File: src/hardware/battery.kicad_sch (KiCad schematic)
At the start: 1 part

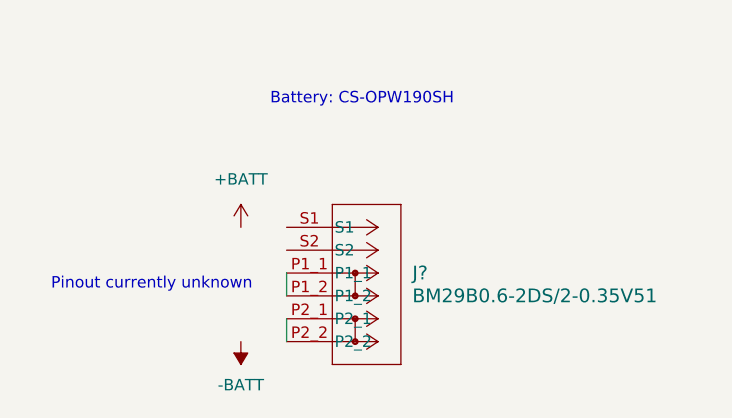
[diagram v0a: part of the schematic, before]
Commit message: Cleanup & Fixes; Added footprints; Removed Light sensors
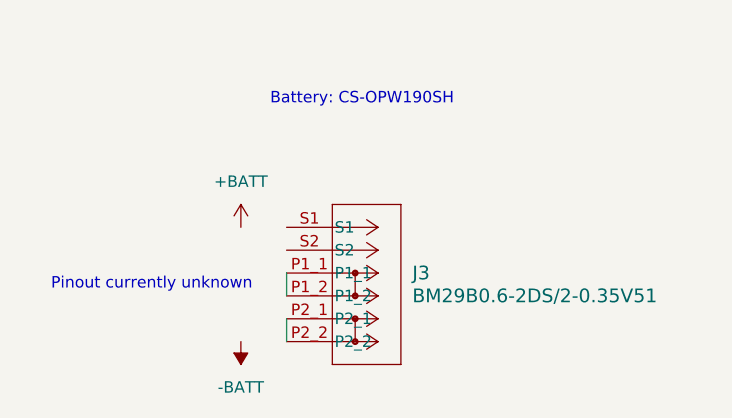
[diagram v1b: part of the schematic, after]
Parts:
- J3: renamed from J?; footprint CONN_BM29B0.6-2DS/2-0.35V51_HIR -> Project:CONN_BM29B0.6-2DS&slash_2-0.35V51_HIR
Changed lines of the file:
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@@
 		(dnp no)
 		(fields_autoplaced yes)
-		(property "Reference" "J?"
+		(property "Reference" "J3"
 			(at 157.48 100.3299 0)
 			(effects
@@
 			)
 		)
-		(property "Footprint" "CONN_BM29B0.6-2DS/2-0.35V51_HIR"
+		(property "Footprint" "Project:CONN_BM29B0.6-2DS&slash_2-0.35V51_HIR"
 			(at 143.51 95.25 0)
 			(effects
@@
 			(project "raywatch"
 				(path "/7b654ee8-2a53-4d39-8b7d-32c7bb3cb0ed/6e6a70ea-4db2-4b59-a2d7-c468f9b8b5a6/0e8527e5-475a-4be8-8e89-500ec2c68fe4"
-					(reference "J?")
+					(reference "J3")
 					(unit 1)
 				)
@@
 		(dnp no)
 		(fields_autoplaced yes)
-		(property "Reference" "#PWR0401"
+		(property "Reference" "#PWR0404"
 			(at 138.43 99.06 0)
 			(effects
@@
 		)
 		(property "Value" "+BATT"
-			(at 138.43 89.916 0)
+			(at 138.43 90.17 0)
 			(effects
 				(font
@@
 			(project "raywatch"
 				(path "/7b654ee8-2a53-4d39-8b7d-32c7bb3cb0ed/6e6a70ea-4db2-4b59-a2d7-c468f9b8b5a6/0e8527e5-475a-4be8-8e89-500ec2c68fe4"
-					(reference "#PWR0401")
+					(reference "#PWR0404")
 					(unit 1)
 				)
@@
 		(dnp no)
 		(fields_autoplaced yes)
-		(property "Reference" "#PWR0402"
+		(property "Reference" "#PWR0405"
 			(at 138.43 104.14 0)
 			(effects
@@
 		)
 		(property "Value" "-BATT"
-			(at 138.43 112.776 0)
+			(at 138.43 113.03 0)
 			(effects
 				(font
@@
 			(project "raywatch"
 				(path "/7b654ee8-2a53-4d39-8b7d-32c7bb3cb0ed/6e6a70ea-4db2-4b59-a2d7-c468f9b8b5a6/0e8527e5-475a-4be8-8e89-500ec2c68fe4"
-					(reference "#PWR0402")
+					(reference "#PWR0405")
 					(unit 1)
 				)

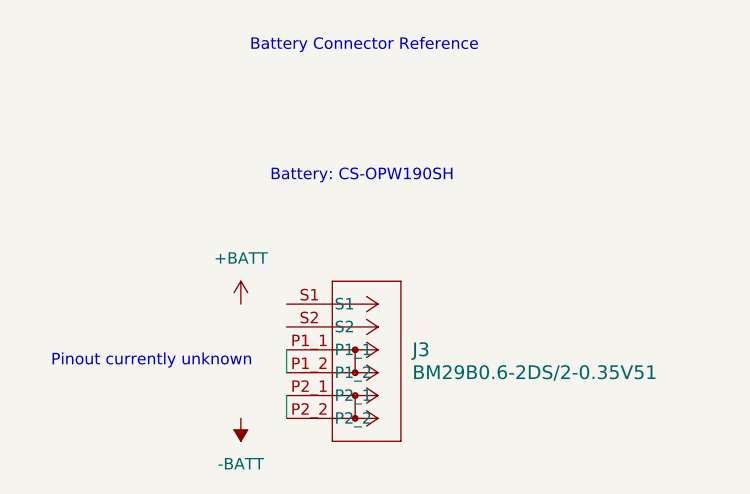
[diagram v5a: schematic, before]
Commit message: Mapped battery pinout; Removed thermistor from PCB, now using thermistor in battery pack
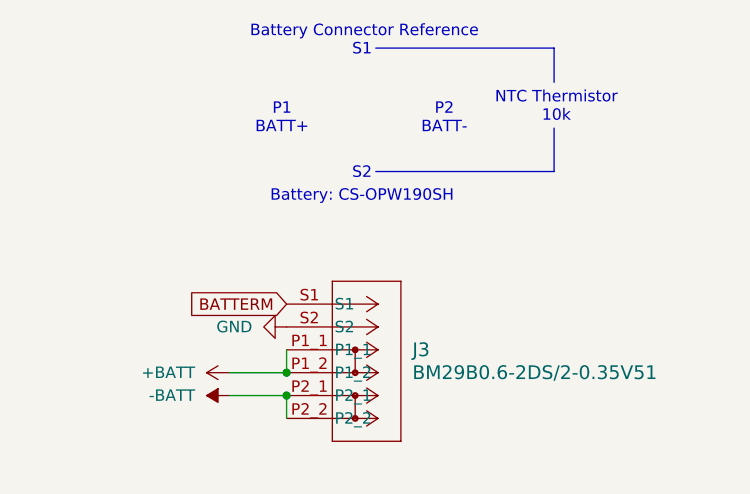
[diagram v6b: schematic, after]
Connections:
- net +BATT: now also J3.P1_1, J3.P1_2
- net -BATT: now also J3.P2_1, J3.P2_2
- net BATTERM: now reaches J3.S1
- net GND: now reaches J3.S2
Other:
- note added: "NTC Thermistor 10k"
- note added: "P1 BATT+"
- note added: "P2 BATT-"
- note added: "S1"
- note added: "S2"
- note removed: "Pinout currently unknown"
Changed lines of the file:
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@@
 		(date "2026-10-21")
 	)
-	(text "Battery: CS-OPW190SH"
-		(exclude_from_sim no)
-		(at 151.892 81.026 0)
+	(text "S1"
+		(exclude_from_sim no)
+		(at 151.892 67.056 0)
 		(effects
 			(font
@@
 		)
 	)
-	(text "Pinout currently unknown"
-		(exclude_from_sim no)
-		(at 128.524 101.6 0)
+	(text "Battery: CS-OPW190SH"
+		(exclude_from_sim no)
+		(at 151.892 83.312 0)
 		(effects
 			(font
@@
 	(text "Battery Connector Reference"
 		(exclude_from_sim no)
-		(at 152.146 66.548 0)
+		(at 152.146 65.024 0)
 		(effects
 			(font
@@
 		)
 	)
+	(text "NTC Thermistor\n10k"
+		(exclude_from_sim no)
+		(at 173.482 73.406 0)
+		(effects
+			(font
+				(size 1.27 1.27)
+			)
+		)
+	)
+	(text "S2"
+		(exclude_from_sim no)
+		(at 151.892 80.772 0)
+		(effects
+			(font
+				(size 1.27 1.27)
+			)
+		)
+	)
+	(text "P1\nBATT+"
+		(exclude_from_sim no)
+		(at 143.002 74.676 0)
+		(effects
+			(font
+				(size 1.27 1.27)
+			)
+		)
+	)
+	(text "P2\nBATT-"
+		(exclude_from_sim no)
+		(at 161.036 74.676 0)
+		(effects
+			(font
+				(size 1.27 1.27)
+			)
+		)
+	)
+	(junction
+		(at 143.51 102.87)
+		(diameter 0)
+		(color 0 0 0 0)
+	)
+	(junction
+		(at 143.51 105.41)
+		(diameter 0)
+		(color 0 0 0 0)
+	)
+	(wire
+		(pts
+			(xy 137.16 105.41) (xy 143.51 105.41)
+		)
+		(stroke
+			(width 0)
+			(type default)
+		)
+	)
+	(wire
+		(pts
+			(xy 137.16 102.87) (xy 143.51 102.87)
+		)
+		(stroke
+			(width 0)
+			(type default)
+		)
+	)
+	(wire
+		(pts
+			(xy 143.51 102.87) (xy 143.51 100.33)
+		)
+		(stroke
+			(width 0)
+			(type default)
+		)
+	)
+	(polyline
+		(pts
+			(xy 173.228 66.802) (xy 153.416 66.802)
+		)
+		(stroke
+			(width 0)
+			(type default)
+		)
+	)
+	(polyline
+		(pts
+			(xy 173.228 80.518) (xy 173.228 75.692)
+		)
+		(stroke
+			(width 0)
+			(type default)
+		)
+	)
 	(wire
 		(pts
@@
 		)
 	)
-	(wire
+	(polyline
 		(pts
-			(xy 143.51 100.33) (xy 143.51 102.87)
+			(xy 153.416 80.518) (xy 173.228 80.518)
+		)
+		(stroke
+			(width 0)
+			(type default)
+		)
+	)
+	(polyline
+		(pts
+			(xy 173.228 70.612) (xy 173.228 66.802)
 		)
 		(stroke
@@
 		)
 	)
+	(global_label "BATTERM"
+		(shape input)
+		(at 143.51 95.25 180)
+		(fields_autoplaced yes)
+		(effects
+			(font
+				(size 1.27 1.27)
+			)
+			(justify right)
+		)
+		(property "Intersheetrefs" "${INTERSHEET_REFS}"
+			(at 132.3606 95.25 0)
+			(effects
+				(font
+					(size 1.27 1.27)
+				)
+				(justify right)
+				(hide yes)
+			)
+		)
+	)
+	(symbol
+		(lib_id "power:GND")
+		(at 143.51 97.79 270)
+		(unit 1)
+		(exclude_from_sim no)
+		(in_bom yes)
+		(on_board yes)
+		(dnp no)
+		(fields_autoplaced yes)
+		(property "Reference" "#PWR072"
+			(at 137.16 97.79 0)
+			(effects
+				(font
+					(size 1.27 1.27)
+				)
+				(hide yes)
+			)
+		)
+		(property "Value" "GND"
+			(at 139.7 97.7899 90)
+			(effects
+				(font
+					(size 1.27 1.27)
+				)
+				(justify right)
+			)
+		)
+		(property "Footprint" ""
+			(at 143.51 97.79 0)
+			(effects
+				(font
+					(size 1.27 1.27)
+				)
+				(hide yes)
+			)
+		)
+		(property "Datasheet" ""
+			(at 143.51 97.79 0)
+			(effects
+				(font
+					(size 1.27 1.27)
+				)
+				(hide yes)
+			)
+		)
+		(property "Description" "Power symbol creates a global label with name \"GND\" , ground"
+			(at 143.51 97.79 0)
+			(effects
+				(font
+					(size 1.27 1.27)
+				)
+				(hide yes)
+			)
+		)
+		(pin "1"
+		)
+		(instances
+			(project "raywatch"
+				(path "/7b654ee8-2a53-4d39-8b7d-32c7bb3cb0ed/81388ce1-b713-4a4d-a62f-b5a425cee66d"
+					(reference "#PWR072")
+					(unit 1)
+				)
+			)
+		)
+	)
 	(symbol
 		(lib_id "BM29B0.6-2DS_2-0.35V51:BM29B0.6-2DS_2-0.35V51")
@@
 	)
 	(symbol
-		(lib_id "power:+BATT")
-		(at 138.43 95.25 0)
+		(lib_id "power:-BATT")
+		(at 137.16 105.41 90)
 		(unit 1)
 		(exclude_from_sim no)
@@
 		(dnp no)
 		(fields_autoplaced yes)
-		(property "Reference" "#PWR0353"
-			(at 138.43 99.06 0)
-			(effects
-				(font
-					(size 1.27 1.27)
-				)
-				(hide yes)
-			)
-		)
-		(property "Value" "+BATT"
-			(at 138.43 90.17 0)
-			(effects
-				(font
-					(size 1.27 1.27)
-				)
+		(property "Reference" "#PWR070"
+			(at 140.97 105.41 0)
+			(effects
+				(font
+					(size 1.27 1.27)
+				)
+				(hide yes)
+			)
+		)
+		(property "Value" "-BATT"
+			(at 133.35 105.4099 90)
+			(effects
+				(font
+					(size 1.27 1.27)
+				)
+				(justify left)
 			)
 		)
 		(property "Footprint" ""
-			(at 138.43 95.25 0)
+			(at 137.16 105.41 0)
 			(effects
 				(font
@@
 		)
 		(property "Datasheet" ""
-			(at 138.43 95.25 0)
-			(effects
-				(font
-					(size 1.27 1.27)
-				)
-				(hide yes)
-			)
-		)
-		(property "Description" "Power symbol creates a global label with name \"+BATT\""
-			(at 138.43 95.25 0)
+			(at 137.16 105.41 0)
+			(effects
+				(font
+					(size 1.27 1.27)
+				)
+				(hide yes)
+			)
+		)
+		(property "Description" "Power symbol creates a global label with name \"-BATT\""
+			(at 137.16 105.41 0)
 			(effects
 				(font
@@
 			(project "raywatch"
 				(path "/7b654ee8-2a53-4d39-8b7d-32c7bb3cb0ed/81388ce1-b713-4a4d-a62f-b5a425cee66d"
-					(reference "#PWR0353")
+					(reference "#PWR070")
 					(unit 1)
 				)
@@
 	)
 	(symbol
-		(lib_id "power:-BATT")
-		(at 138.43 107.95 180)
+		(lib_id "power:+BATT")
+		(at 137.16 102.87 90)
 		(unit 1)
 		(exclude_from_sim no)
@@
 		(dnp no)
 		(fields_autoplaced yes)
-		(property "Reference" "#PWR0354"
-			(at 138.43 104.14 0)
-			(effects
-				(font
-					(size 1.27 1.27)
-				)
-				(hide yes)
-			)
-		)
-		(property "Value" "-BATT"
-			(at 138.43 113.03 0)
-			(effects
-				(font
-					(size 1.27 1.27)
-				)
+		(property "Reference" "#PWR071"
+			(at 140.97 102.87 0)
+			(effects
+				(font
+					(size 1.27 1.27)
+				)
+				(hide yes)
+			)
+		)
+		(property "Value" "+BATT"
+			(at 133.35 102.8699 90)
+			(effects
+				(font
+					(size 1.27 1.27)
+				)
+				(justify left)
 			)
 		)
 		(property "Footprint" ""
-			(at 138.43 107.95 0)
+			(at 137.16 102.87 0)
 			(effects
 				(font
@@
 		)
 		(property "Datasheet" ""
-			(at 138.43 107.95 0)
-			(effects
-				(font
-					(size 1.27 1.27)
-				)
-				(hide yes)
-			)
-		)
-		(property "Description" "Power symbol creates a global label with name \"-BATT\""
-			(at 138.43 107.95 0)
+			(at 137.16 102.87 0)
+			(effects
+				(font
+					(size 1.27 1.27)
+				)
+				(hide yes)
+			)
+		)
+		(property "Description" "Power symbol creates a global label with name \"+BATT\""
+			(at 137.16 102.87 0)
 			(effects
 				(font
@@
 			(project "raywatch"
 				(path "/7b654ee8-2a53-4d39-8b7d-32c7bb3cb0ed/81388ce1-b713-4a4d-a62f-b5a425cee66d"
-					(reference "#PWR0354")
+					(reference "#PWR071")
 					(unit 1)
 				)

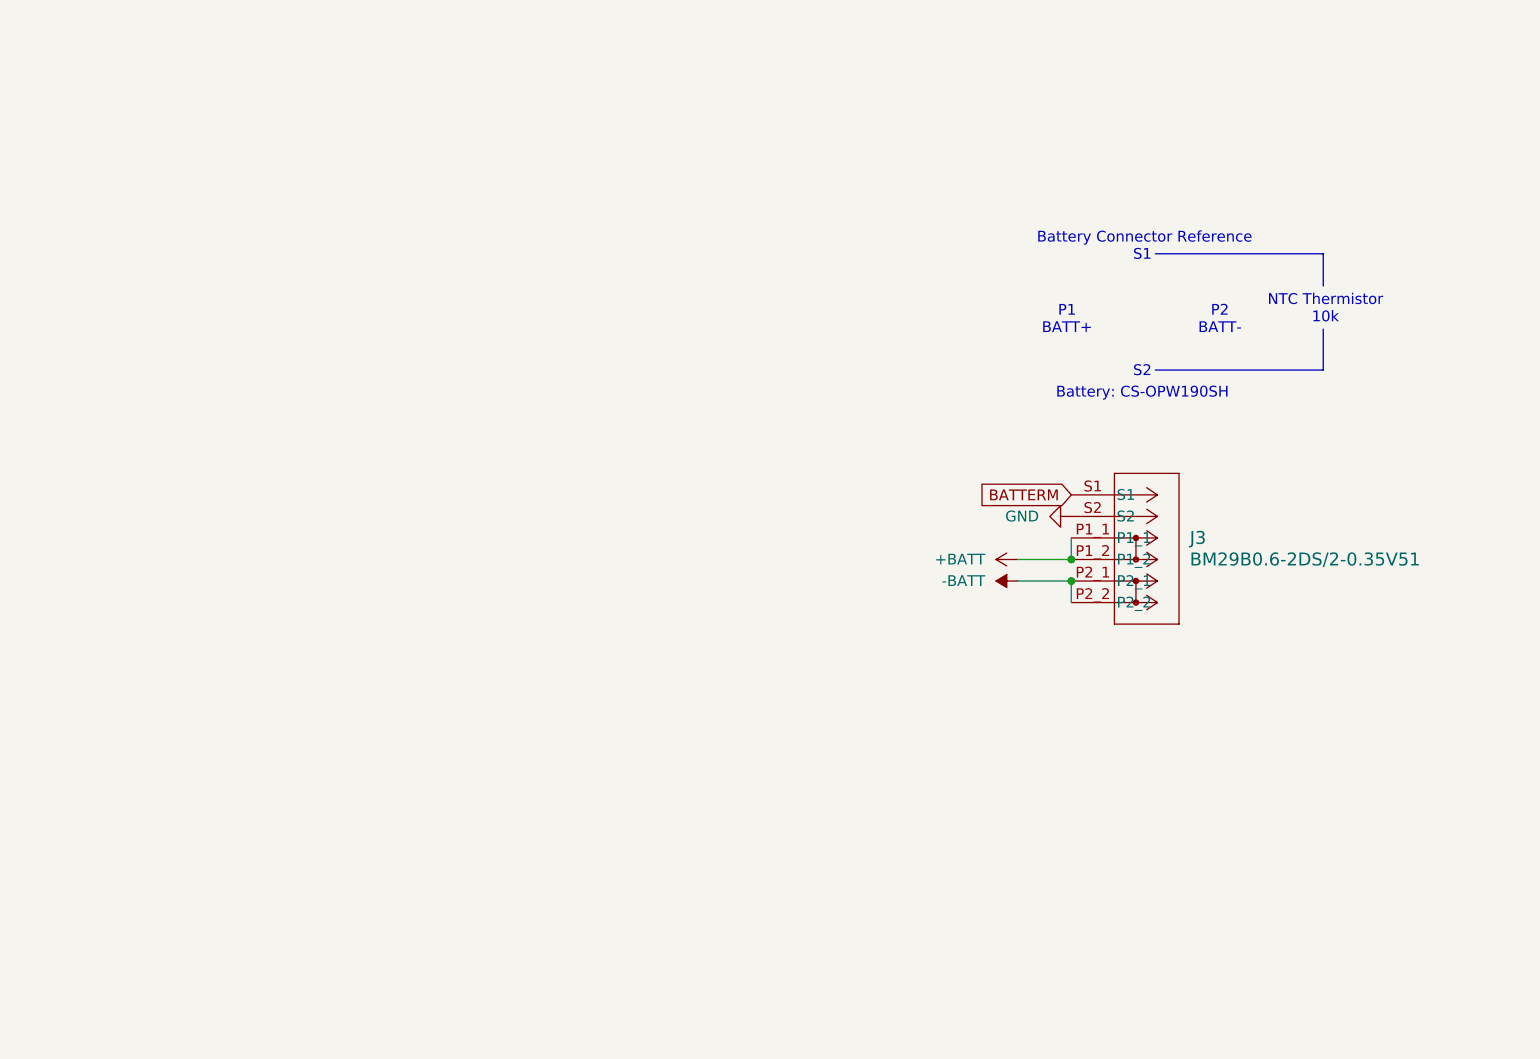
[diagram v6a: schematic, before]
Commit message: Replaced global labels with pin headers
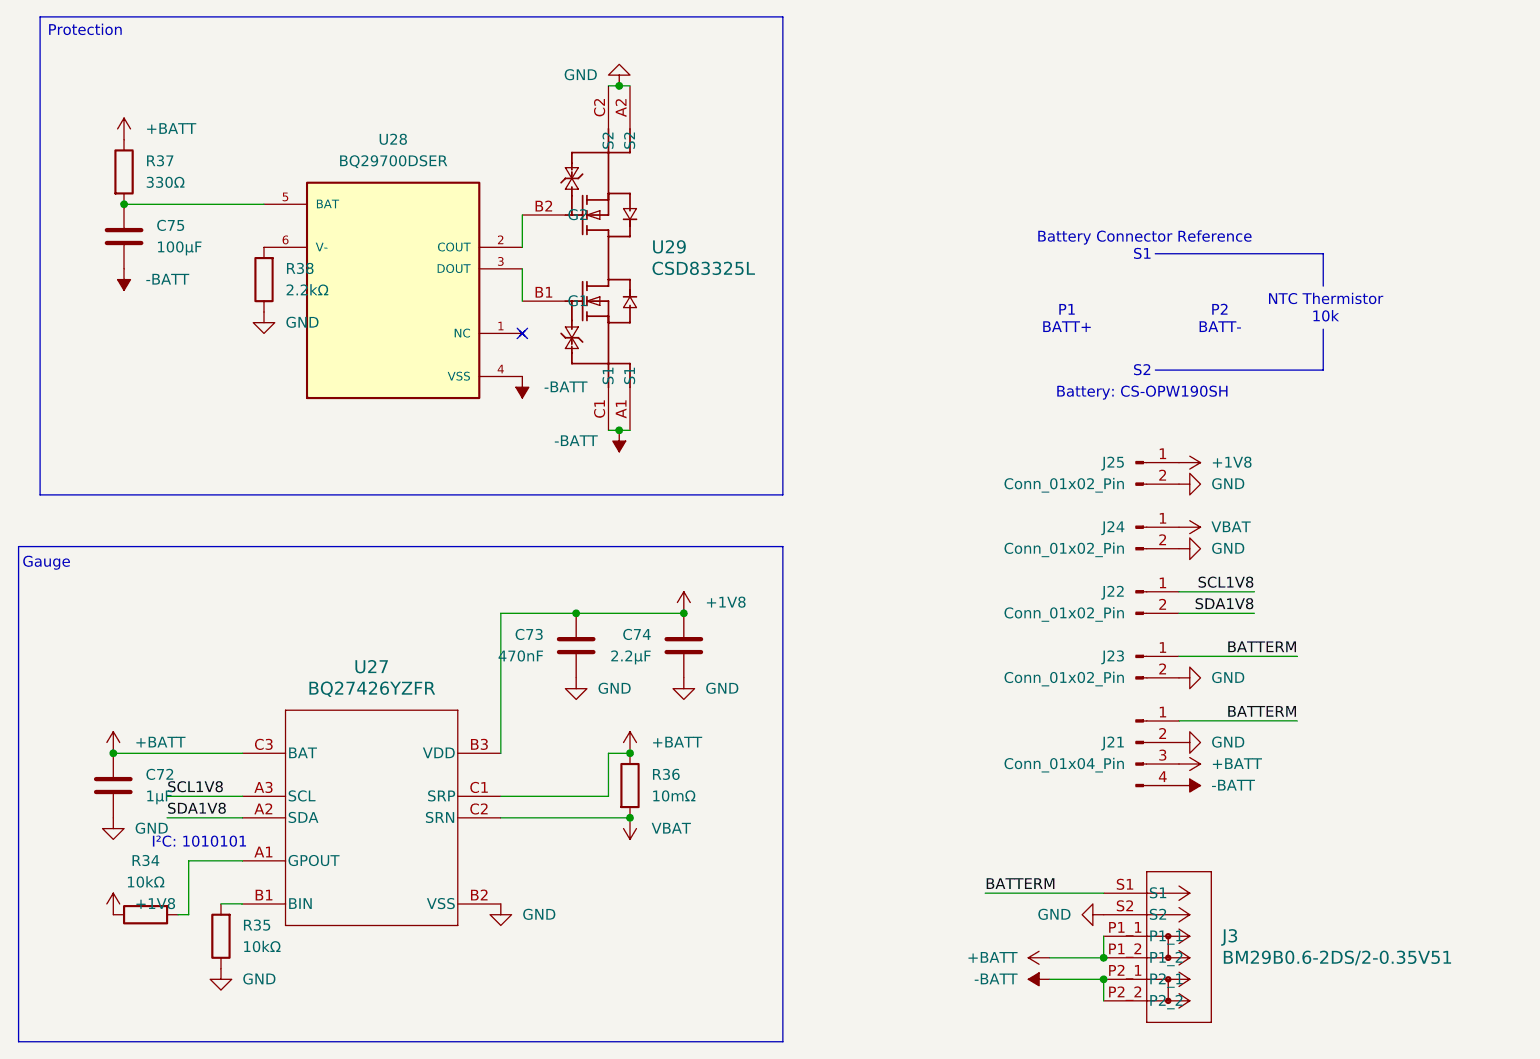
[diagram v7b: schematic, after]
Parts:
- added C72: 1µF, Capacitor_SMD:C_0504_1310Metric, symbol Device:C
- added C73: 470nF, Capacitor_SMD:C_0504_1310Metric, symbol Device:C
- added C74: 2.2µF, Capacitor_SMD:C_0504_1310Metric, symbol Device:C
- added C75: 100µF, Capacitor_SMD:C_0504_1310Metric, symbol Device:C
- added J21: Conn_01x04_Pin, symbol Connector:Conn_01x04_Pin
- added J22, J23, J24, J25: Conn_01x02_Pin, symbol Connector:Conn_01x02_Pin
- added R34, R35: 10kΩ, Resistor_SMD:R_0402_1005Metric, symbol Device:R
- added R36: 10mΩ, Resistor_SMD:R_0402_1005Metric, symbol Device:R
- added R37: 330Ω, Resistor_SMD:R_0402_1005Metric, symbol Device:R
- added R38: 2.2kΩ, Resistor_SMD:R_0402_1005Metric, symbol Device:R
- added U27: BQ27426YZFR, Project:IC_BQ27421YZFR-G1A, symbol BQ27426YZFR:BQ27426YZFR
- added U28: BQ29700DSER, Project:SON50P150X150X80-6N, symbol BQ29700DSER:BQ29700DSER
- added U29: CSD83325L, Project:YJE0006A, symbol CSD83325L:CSD83325L
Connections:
- net +BATT: now also C72.2, J21.3 (Pin_3), R36.1, R37.1, U27.C1 (SRP), U27.C3 (BAT)
- net -BATT: now also C75.2, J21.4 (Pin_4), U28.4 (VSS), U29.A1 (S1), U29.C1 (S1)
- net BATTERM: now also J21.1 (Pin_1), J23.1 (Pin_1)
- net GND: now also C72.1, C73.1, C74.1, J21.2 (Pin_2), J23.2 (Pin_2), J24.2 (Pin_2), J25.2 (Pin_2), R35.1, R38.1, U27.B2 (VSS), U29.A2 (S2), U29.C2 (S2)
- new net: C75.1, R37.2, U28.5 (BAT)
- new net: R34.2, U27.A1 (GPOUT)
- new net: U28.2 (COUT), U29.B2 (G2)
- new net: U28.3 (DOUT), U29.B1 (G1)
- new net: R38.2, U28.6 (V-)
- new net: R35.2, U27.B1 (BIN)
- new net +1V8: C73.2, C74.2, J25.1 (Pin_1), R34.1, U27.B3 (VDD)
- new net SCL1V8: J22.1 (Pin_1), U27.A3 (SCL)
- new net SDA1V8: J22.2 (Pin_2), U27.A2 (SDA)
- new net VBAT: J24.1 (Pin_1), R36.2, U27.C2 (SRN)
- no-connect marks 0 -> 1
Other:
- note added: "Gauge"
- note added: "I²C: 1010101"
- note added: "Protection"
- moved on the sheet: J3

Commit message: Reannotated schematic
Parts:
- renumbered C72 to C67, C75 to C68, C73 to C69, C74 to C70, J3 to J76, J25 to J77, J24 to J78, J22 to J79, J23 to J80, J21 to J81, R37 to R28, R34 to R29, R35 to R30, R38 to R31, R36 to R32, U27 to U28, U28 to U29, U29 to U30
